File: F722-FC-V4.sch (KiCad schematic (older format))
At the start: 8 parts, among them J13 USB_B_Micro

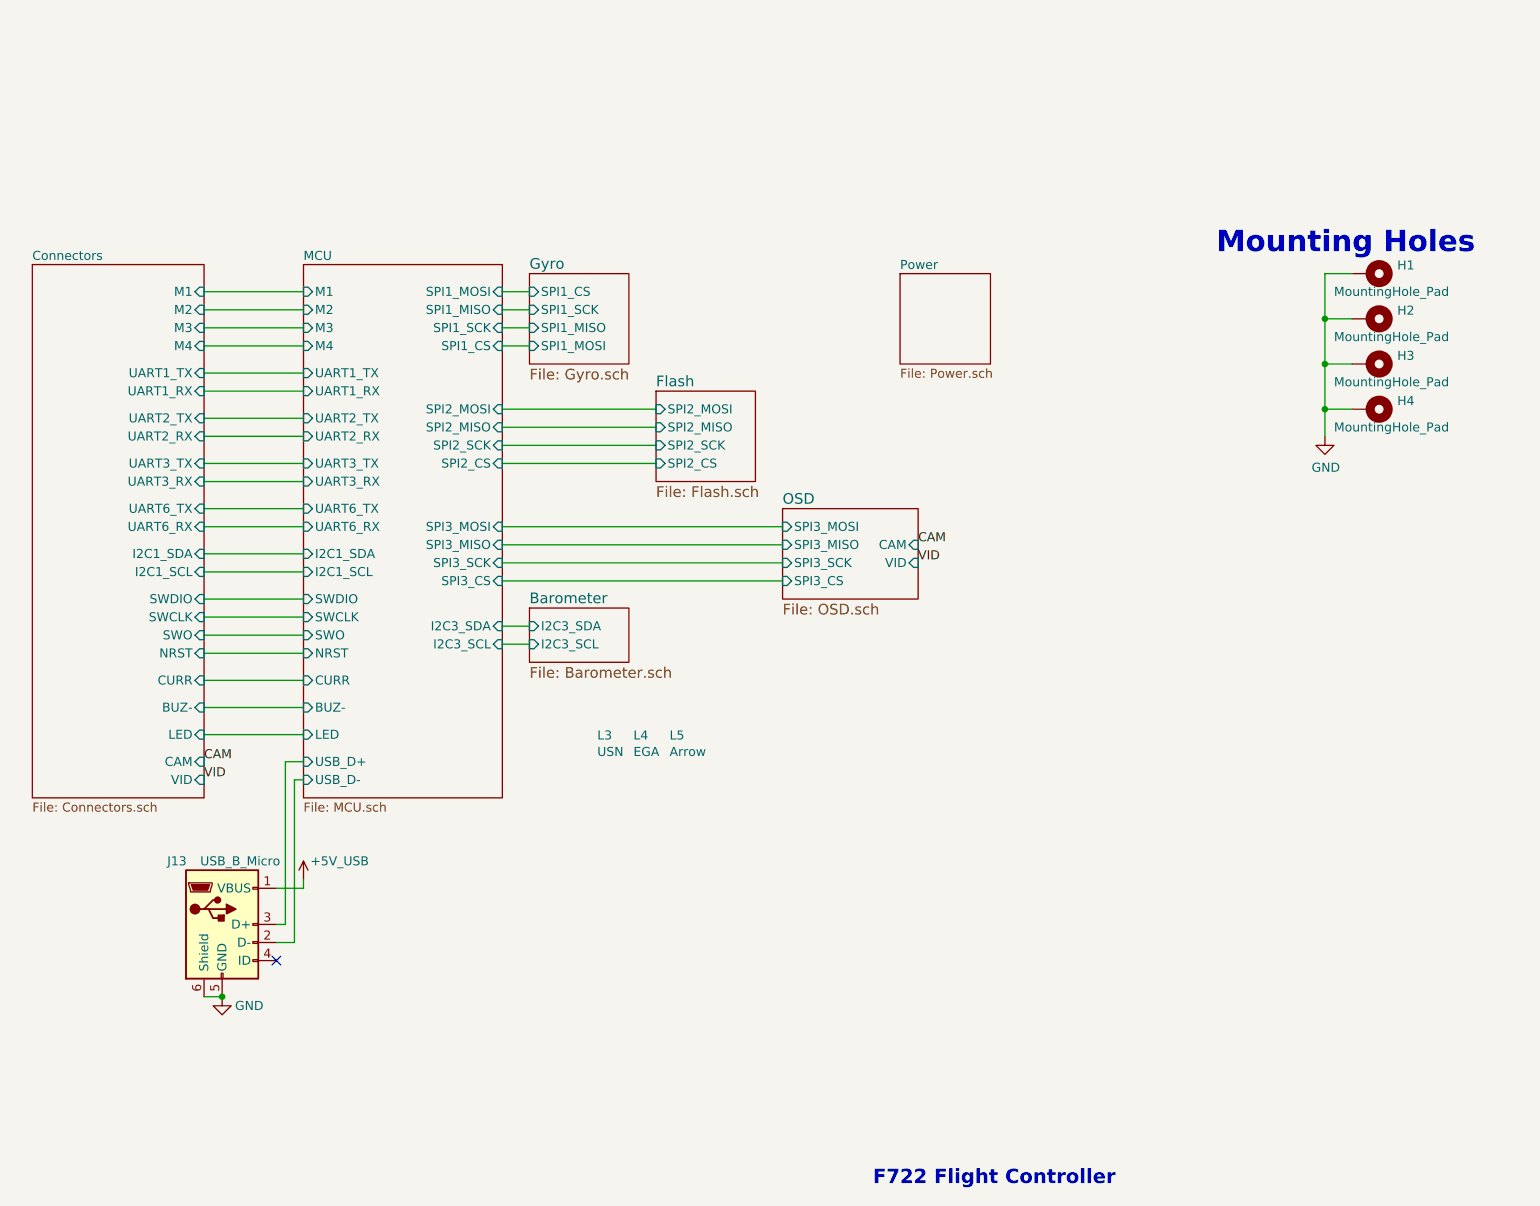
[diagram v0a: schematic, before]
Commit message: Updated the schematics to include pictures
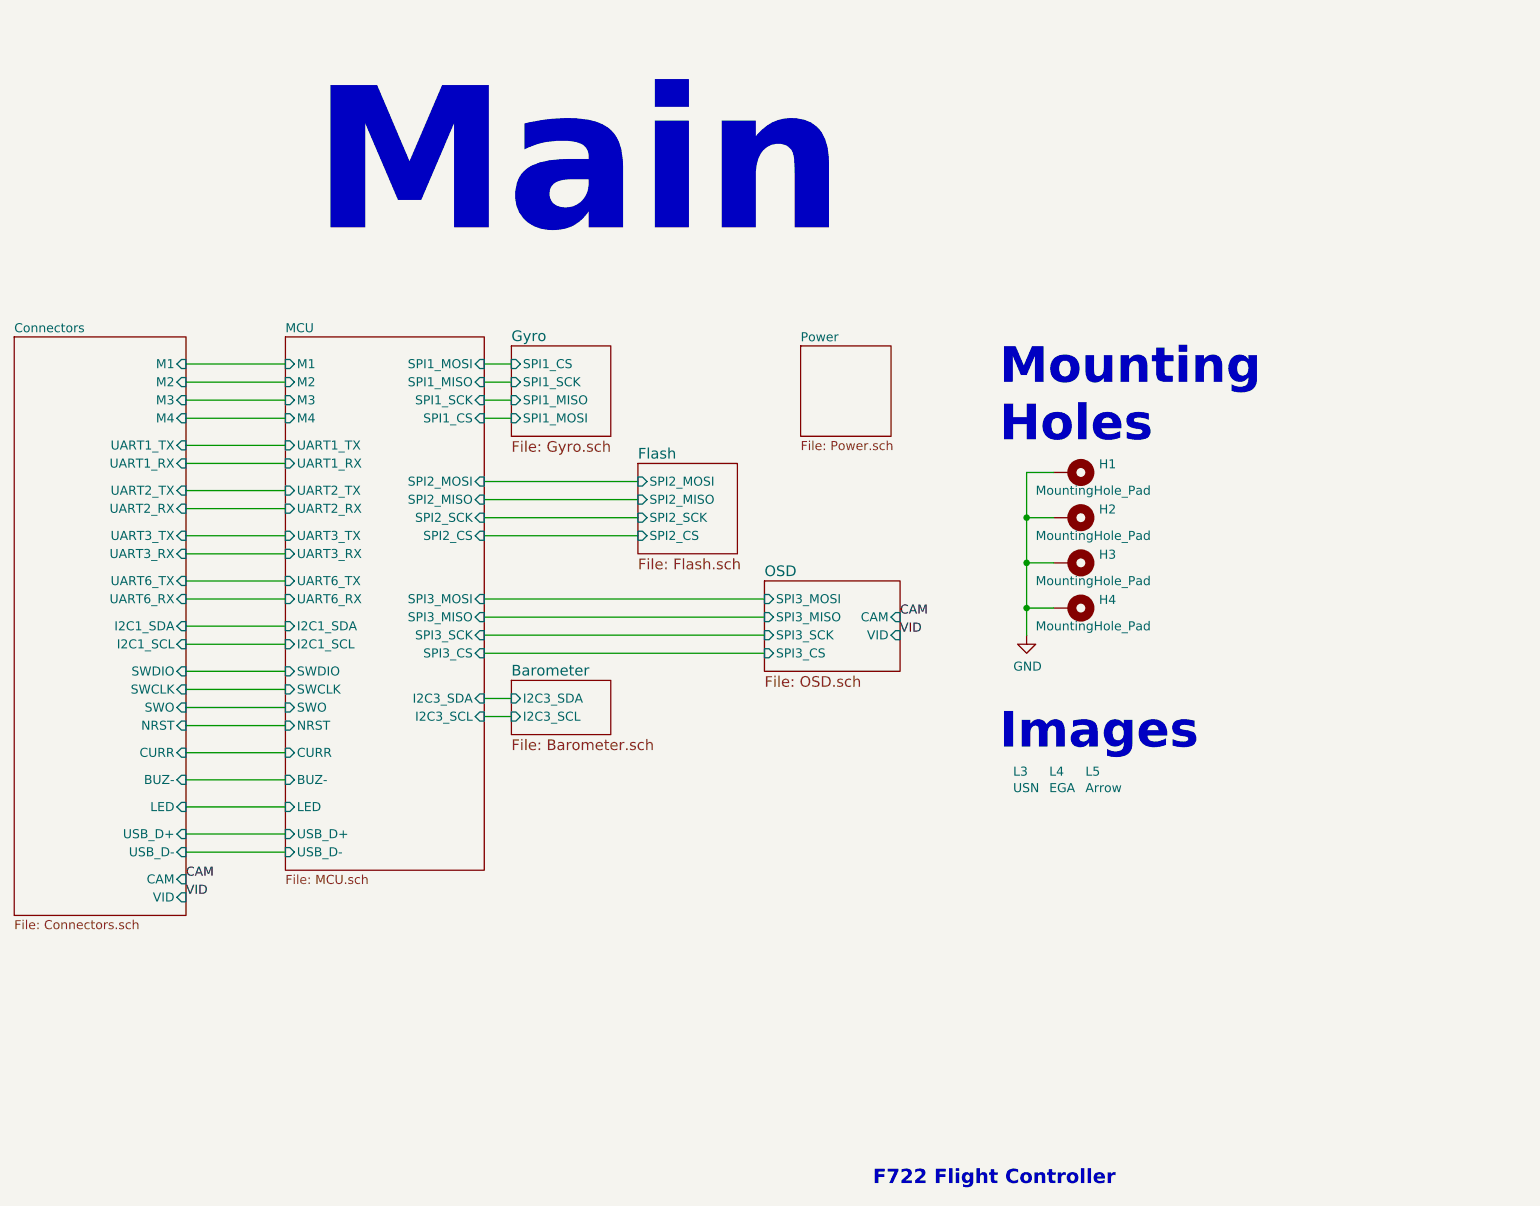
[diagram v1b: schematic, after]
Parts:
- removed J13: USB_B_Micro, Connector_USB:USB_Micro-B_Amphenol_10103594-0001LF_Horizontal, symbol Connector:USB_B_Micro
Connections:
- no-connect marks 1 -> 0
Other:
- note added: "Images"
- note added: "Main"
- note added: "Mounting \nHoles"
- note removed: "Mounting Holes"
- moved on the sheet: H1, H2, H3, H4
